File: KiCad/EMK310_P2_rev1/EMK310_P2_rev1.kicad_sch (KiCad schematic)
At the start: 65 parts, among them J1 Conn_01x20_Socket, J2 Conn_01x02_Socket, J3 Conn_01x02_Socket, J4 Conn_01x20_Socket, J5 Conn_01x05_Socket, J6 Conn_01x04_Socket, U1 PIC18F45K22, U2 Opamp_Quad, U3 Opamp_Dual, U4 MCP2221AxP

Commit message: Updated PCB Design
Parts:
- removed U4: MCP2221AxP, Package_DIP:DIP-14_W7.62mm, symbol Interface_USB:MCP2221AxP
- removed Wf1: Conn_02x04_Counter_Clockwise, Connector_PinHeader_2.54mm:PinHeader_2x04_P2.54mm_Vertical, symbol Connector_Generic:Conn_02x04_Counter_Clockwise
- added J7: Conn_01x02_Socket, Connector_PinHeader_2.54mm:PinHeader_1x02_P2.54mm_Vertical, symbol Connector:Conn_01x02_Socket
- added RF1: ESP-01-Wifi, Jan-Hendrik:PinHeader_2x04_P2.54mm_Vertical_Antenna, symbol Jan-Hendrik:ESP-01-Wifi
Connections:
- net +9V: now also J7.1 (Pin_1)
- net GNDREF: now also AFF1.5 (DP), D1.3 (K), D2.3 (K), D3.3 (K), D4.3 (K), D5.3 (K), J6.4 (Pin_4), J7.2 (Pin_2), RF1.1 (GND)
- net MOTOR_1_B: now also J4.20 (Pin_20), U1.20 (RD1); no longer J4.10 (Pin_10), U1.10 (RE2)
- net MOTOR_1_F: now also J4.10 (Pin_10), U1.10 (RE2); no longer J4.8 (Pin_8), U1.8 (RE0)
- net MOTOR_2_F: now also J4.8 (Pin_8), U1.8 (RE0); no longer J1.8 (Pin_8), U1.33 (RB0)
- net Vdd: now also RF1.8 (Vcc)
- net at D8.2 (A), R18.1, U2.5 (+): now also J5.4 (Pin_4); no longer J5.3 (Pin_3)
- net at J1.20 (Pin_20), U1.21 (RD2): now also R31.2; no longer R30.2
- net at D9.2 (A), R19.1, U2.3 (+): now also J5.5 (Pin_5); no longer J5.4 (Pin_4)
- net at J1.19 (Pin_19), U1.22 (RD3): now also R30.2; no longer R29.2
- net at J1.14 (Pin_14), U1.27 (RD4): now also R29.2; no longer R28.2
- net at J1.13 (Pin_13), U1.28 (RD5): now also R28.2; no longer R27.2
- net at J1.12 (Pin_12), U1.29 (RD6): now also R27.2; no longer R26.2
- net at J1.11 (Pin_11), U1.30 (RD7): now also R26.2
- net at J1.1 (Pin_1), U1.40 (RB7/PGD): now also RF1.7 (U0RXD)
- net at D10.2 (A), R20.1, U3.5 (+): now also J5.3 (Pin_3); no longer J5.5 (Pin_5)
- new net: J1.8 (Pin_8), U1.33 (RB0)
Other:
- moved on the sheet: U2E, U3C

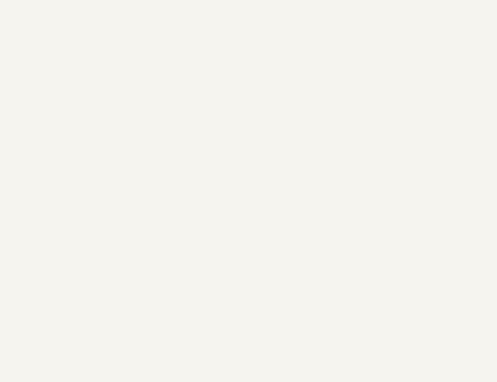
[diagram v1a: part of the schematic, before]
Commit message: Added mounting Holes to PCB design
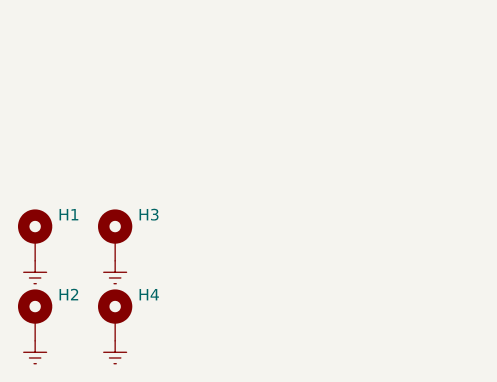
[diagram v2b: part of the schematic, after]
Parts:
- added H1, H2, H3, H4: MountingHole_Pad, MountingHole:MountingHole_3.2mm_M3_DIN965_Pad, symbol Mechanical:MountingHole_Pad
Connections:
- net GNDREF: now also H1.1, H2.1, H3.1, H4.1

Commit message: work
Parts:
- removed RF1: ESP-01-Wifi, Jan-Hendrik:PinHeader_2x04_P2.54mm_Vertical_Antenna, symbol Jan-Hendrik:ESP-01-Wifi
- added C6, C7: 0.22uF, Capacitor_THT:C_Rect_L9.0mm_W2.5mm_P7.50mm_MKT, symbol Device:C
- added C8: 0.22uF, Capacitor_THT:C_Rect_L9.0mm_W2.5mm_P7.50mm_MKT, symbol Device:C_Small
- added J8: USB_A, Connector_USB:USB_A_Connfly_DS1095, symbol Connector:USB_A
- added Q1, Q2, Q3: VP0610L, Package_TO_SOT_THT:TO-92L_Inline, symbol Transistor_FET:VP0610L
- added R33, R34, R35: 10k, Resistor_THT:R_Axial_DIN0207_L6.3mm_D2.5mm_P10.16mm_Horizontal, symbol Device:R
- added U4: MCP2221AxP, Package_DIP:DIP-14_W7.62mm, symbol Interface_USB:MCP2221AxP
- C5: value C_Small -> 10uF
- H1, H2, H3, H4: footprint MountingHole:MountingHole_3.2mm_M3_DIN965_Pad -> MountingHole:MountingHole_2.2mm_M2_DIN965_Pad_TopOnly
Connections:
- net +9V: now also C8.2
- net GNDREF: now also U3.3 (+), C6.2, C7.2, C8.1, J8.4 (GND), J8.5 (Shield), U4.14 (VSS)
- net LEDB: now also Q3.2 (G); no longer J6.3 (Pin_3), R12.2, R15.2, R3.2, R6.2, R9.2
- net LEDG: now also Q2.2 (G); no longer J6.2 (Pin_2), R11.2, R14.2, R2.2, R5.2, R8.2
- net LEDR: now also Q1.2 (G); no longer J6.1 (Pin_1), R1.2, R10.2, R13.2, R4.2, R7.2
- net Vdd: now also Q1.1 (S), Q2.1 (S), Q3.1 (S), R33.1, R34.1, R35.1, U4.1 (VDD)
- net at J1.19 (Pin_19), U1.22 (RD3): no longer R30.2
- net at U3.1: now also U3.2 (-)
- net SCL: now reaches J4.19 (Pin_19), U1.19 (RD0)
- net SCL: now also R34.2, U4.10 (SCL); no longer R32.2
- net at J4.1 (Pin_1), U1.1 (RE3/Vp): now also R35.2
- net at J4.14 (Pin_14), U1.14 (RA6/OSC2): now also R26.2
- net at J4.2 (Pin_2), U1.2 (RA0): now also R32.2
- net at J1.20 (Pin_20), U1.21 (RD2): no longer R31.2
- net at J1.14 (Pin_14), U1.27 (RD4): no longer R29.2
- net at J1.13 (Pin_13), U1.28 (RD5): no longer R28.2
- net at J1.12 (Pin_12), U1.29 (RD6): now also U4.5 (URx); no longer R27.2
- net at J4.3 (Pin_3), U1.3 (RA1): now also R31.2
- net at J1.11 (Pin_11), U1.30 (RD7): now also U4.6 (UTx); no longer R26.2
- net at J1.8 (Pin_8), U1.33 (RB0): now also U4.4 (~{RST})
- net SDA: now reaches J1.6 (Pin_6), U1.35 (RB2)
- net SDA: now also R33.2, U4.9 (SDA)
- net at J4.4 (Pin_4), U1.4 (RA2): now also R30.2
- net at J4.5 (Pin_5), U1.5 (RA3): now also R29.2
- net at J4.6 (Pin_6), U1.6 (RA4): now also R28.2
- net at J4.7 (Pin_7), U1.7 (RA5): now also R27.2
- new net: J6.1 (Pin_1), Q1.3 (D), R1.2, R10.2, R13.2, R4.2, R7.2
- new net: J6.2 (Pin_2), Q2.3 (D), R11.2, R14.2, R2.2, R5.2, R8.2
- new net: J6.3 (Pin_3), Q3.3 (D), R12.2, R15.2, R3.2, R6.2, R9.2
- new net: C7.1, U4.11 (VUSB)
- new net: J8.3 (D+), U4.12 (D-)
- new net: J8.2 (D-), U4.13 (D+)
- new net: C6.1, J8.1 (VBUS)
- no-connect marks 8 -> 9
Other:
- moved on the sheet: AFF1, C1, C2, C3, C4, D1, D10, D2, D3, D4, D5, D6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
